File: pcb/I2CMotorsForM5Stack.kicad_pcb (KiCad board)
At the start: 2 copper layers, 60 x 50 mm, 26 parts, among them J1 free_holes, J3 Conn_01x06, J4 Conn_01x06, SW1 SW_DIP_x08, U1 TB6612FNG, U2 ATmega328PB-MU

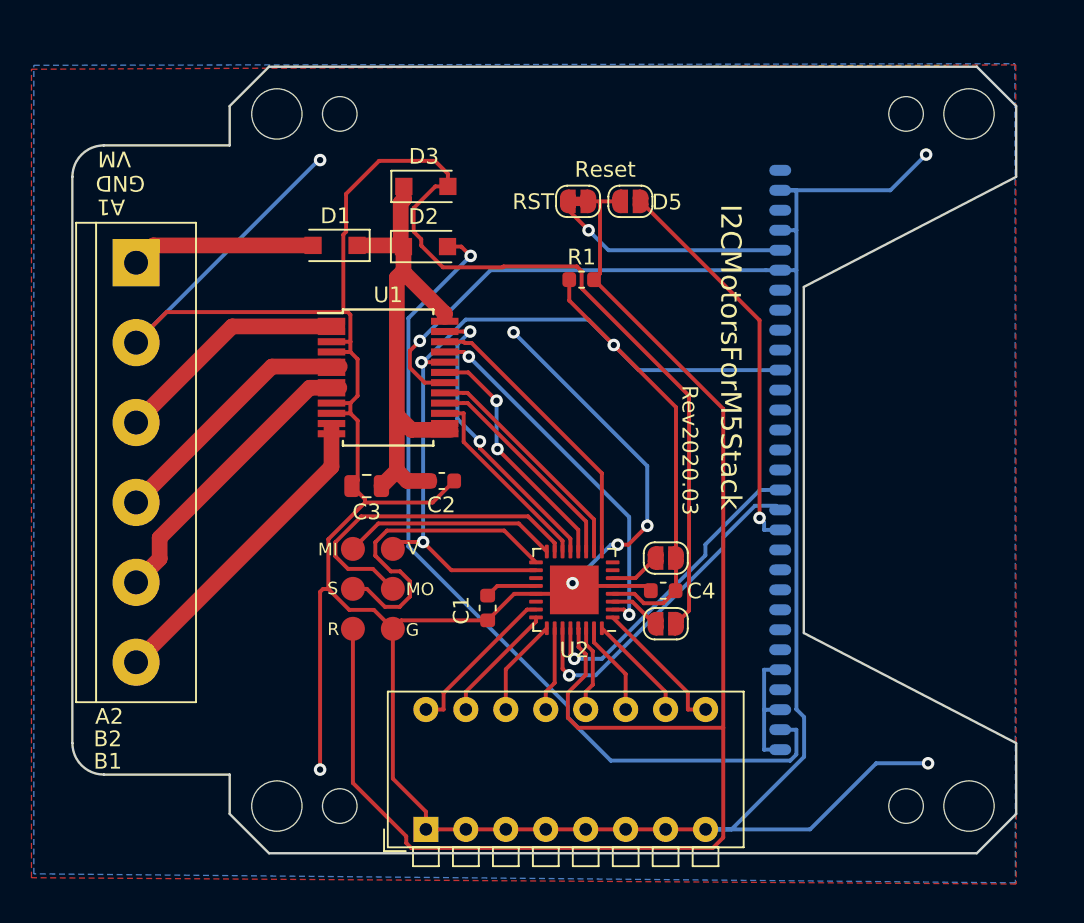
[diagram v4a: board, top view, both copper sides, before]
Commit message: Add connectors and address pads
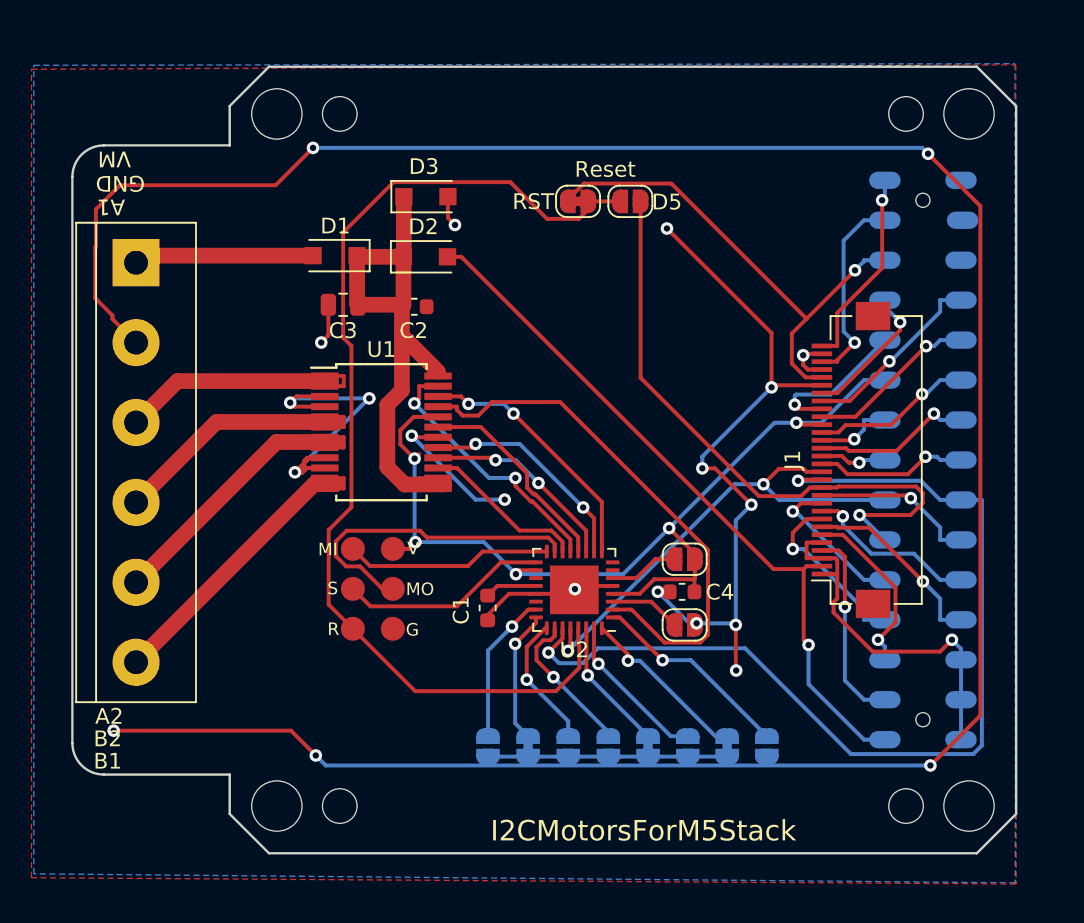
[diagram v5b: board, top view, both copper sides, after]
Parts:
- removed R1: 10k, Resistor_SMD:R_0603_1608Metric
- removed SW1: SW_DIP_x08, Button_Switch_THT:SW_DIP_SPSTx08_Piano_CTS_Series194-8MSTN_W7.62mm_P2.54mm
- added ADDR1: NO, Jumper:SolderJumper-2_P1.3mm_Open_RoundedPad1.0x1.5mm, B.Cu at (116.4, 93.2)
- added ADDR2: NC, Jumper:SolderJumper-2_P1.3mm_Bridged_RoundedPad1.0x1.5mm, B.Cu at (119.0, 93.2)
- added ADDR3: NO, Jumper:SolderJumper-2_P1.3mm_Open_RoundedPad1.0x1.5mm, B.Cu at (121.5, 93.2)
- added ADDR4: NO, Jumper:SolderJumper-2_P1.3mm_Open_RoundedPad1.0x1.5mm, B.Cu at (124.1, 93.2)
- added ADDR5: NC, Jumper:SolderJumper-2_P1.3mm_Bridged_RoundedPad1.0x1.5mm, B.Cu at (126.6, 93.2)
- added ADDR6: NO, Jumper:SolderJumper-2_P1.3mm_Open_RoundedPad1.0x1.5mm, B.Cu at (129.1, 93.2)
- added ADDR7: NC, Jumper:SolderJumper-2_P1.3mm_Bridged_RoundedPad1.0x1.5mm, B.Cu at (131.6, 93.2)
- added ADDR8: NO, Jumper:SolderJumper-2_P1.3mm_Open_RoundedPad1.0x1.5mm, B.Cu at (134.1, 93.2)
- added J2: 2x15socket, my-kicad-footprints:PinSocket_2x15_P2.54mm_Vertical_SMD_just_for_M5Stack_bottom, B.Cu at (144.1, 75.0)
- J1: value free_holes -> FFC_connector; footprint footprints:Pads_1x30_P1.27mm_Vertical -> Connector_FFC-FPC:Hirose_FH12-30S-0.5SH_1x30-1MP_P0.50mm_Horizontal; moved to F.Cu
- JP1: value Jumper_NC_Small -> NC
- JP2: value Jumper_NO_Small -> NO
- JP3, JP4: value NC -> NO
- moved J1 19.0 mm to (139.5, 75.0), turned to 90 degrees
- moved C3 11.6 mm to (107.2, 65.1)
- moved C2 11.2 mm to (111.7, 65.3)
- moved U1 3.50 mm to (109.6, 73.2)
- moved JP3 1.20 mm to (128.9, 85.5)
- moved JP4 1.20 mm to (128.9, 81.3)
- moved C4 1.20 mm to (128.8, 83.4)
- moved D3 0.65 mm to (112.5, 58.3)
- moved D1 0.65 mm to (106.7, 62.0)
- moved D2 0.65 mm to (112.4, 62.1)
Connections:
- J1 pad 1: /35 -> /HPWR
- J1 pad 10: /19 -> /13
- J1 pad 11: +3V3 -> /2
- J1 pad 12: /18 -> /5
- J1 pad 13: /1 -> /21
- J1 pad 14: /3 -> /22
- J1 pad 15: /17 -> /16
- J1 pad 16: /16 -> /17
- J1 pad 17: /22 -> /3
- J1 pad 18: /21 -> /1
- J1 pad 19: /5 -> /18
- J1 pad 2: GND -> +BATT
- J1 pad 20: /2 -> +3V3
- J1 pad 21: /13 -> /19
- J1 pad 22: /12 -> /26
- J1 pad 23: /0 -> /23
- J1 pad 24: /15 -> /25
- J1 pad 25: /34 -> GND
- J1 pad 26: /HPWR -> /RST
- J1 pad 27: +5V -> GND
- J1 pad 28: /HPWR -> /36
- J1 pad 29: +BATT -> GND
- J1 pad 3: /36 -> /HPWR
- J1 pad 30: /HPWR -> /35
- J1 pad 4: GND -> +5V
- J1 pad 5: /RST -> /HPWR
- J1 pad 6: GND -> /34
- J1 pad 7: /25 -> /15
- J1 pad 8: /23 -> /0
- J1 pad 9: /26 -> /12
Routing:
- net GND: track 311.0 -> 267.7 mm, vias 9 -> 22
- net /21: track 21.5 -> 62.5 mm, vias 1 -> 2
- net /SPI_RESET: track 98.1 -> 66.5 mm
- net /RST: track 15.1 -> 31.4 mm
- net /HPWR: track 8.16 -> 23.8 mm, vias 0 -> 1
- net /5: track 25.2 -> 39.9 mm
- net +3V3: track 75.4 -> 61.5 mm, vias 3 -> 5
- net /35: track 0.00 -> 12.8 mm, vias 0 -> 1
- net /36: track 0.00 -> 12.6 mm, vias 0 -> 1
- net +5V: track 0.00 -> 12.5 mm, vias 0 -> 1
- net /15: track 0.00 -> 12.1 mm, vias 0 -> 1
- net /23: track 0.00 -> 11.9 mm, vias 0 -> 1
- net /0: track 0.00 -> 11.4 mm, vias 0 -> 1
- net /34: track 0.00 -> 11.3 mm, vias 0 -> 1
- net /12: track 0.00 -> 11.0 mm, vias 0 -> 1
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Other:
- outline, holes or cut-outs redrawn
- board text added: "Rev2020.04"
- board text removed: "0/MK"
- board text removed: "1/T0"
- board text removed: "12/SK"
- board text removed: "13/WS"
- board text removed: "15/OUT"
- board text removed: "16/R2"
- board text removed: "17/T2"
- board text removed: "18/SCK"
- board text removed: "19/MI"
- board text removed: "2"
- board text removed: "21/SDA"
- board text removed: "22/SCL"
- board text removed: "23/MO"
- board text removed: "25/DA"
- board text removed: "26/DA"
- board text removed: "3/R0"
- board text removed: "34/IN"
- board text removed: "36/AD"
- board text removed: "3V3"
- board text removed: "5"
- board text removed: "5V"
- board text removed: "BAT"
- board text removed: "HPWR"
- board text removed: "Rev2020.03"

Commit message: Change start number for address pad
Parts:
- renumbered ADDR1 to ADDR0, ADDR2 to ADDR1, ADDR3 to ADDR2, ADDR4 to ADDR3, ADDR5 to ADDR4, ADDR6 to ADDR5, ADDR7 to ADDR6, ADDR8 to ADDR7
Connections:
- ADDR0 pad 2: /ADDR1 -> /ADDR0
- ADDR1 pad 2: /ADDR2 -> /ADDR1
- ADDR2 pad 2: /ADDR3 -> /ADDR2
- ADDR3 pad 2: /ADDR4 -> /ADDR3
- ADDR4 pad 2: /ADDR5 -> /ADDR4
- ADDR5 pad 2: /ADDR6 -> /ADDR5
- ADDR6 pad 2: /ADDR7 -> /ADDR6
- ADDR7 pad 2: /ADDR8 -> /ADDR7
- U2 pad 1: /ADDR8 -> /ADDR7
- U2 pad 23: /ADDR1 -> /ADDR0
- U2 pad 24: /ADDR2 -> /ADDR1
- U2 pad 25: /ADDR3 -> /ADDR2
- U2 pad 26: /ADDR4 -> /ADDR3
- U2 pad 30: /ADDR5 -> /ADDR4
- U2 pad 31: /ADDR6 -> /ADDR5
- U2 pad 32: /ADDR7 -> /ADDR6
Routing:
- net /ADDR8: track 12.9 -> 0.00 mm, vias 1 -> 0
- net /ADDR0: track 0.00 -> 10.0 mm, vias 0 -> 1
- net /ADDR7: track 11.0 -> 12.9 mm
- net /ADDR1: track 10.0 -> 8.44 mm
- net /ADDR5: track 8.49 -> 9.97 mm
- net /ADDR6: track 9.97 -> 11.0 mm
- net /ADDR4: track 9.50 -> 8.49 mm
- net /ADDR3: track 8.54 -> 9.50 mm

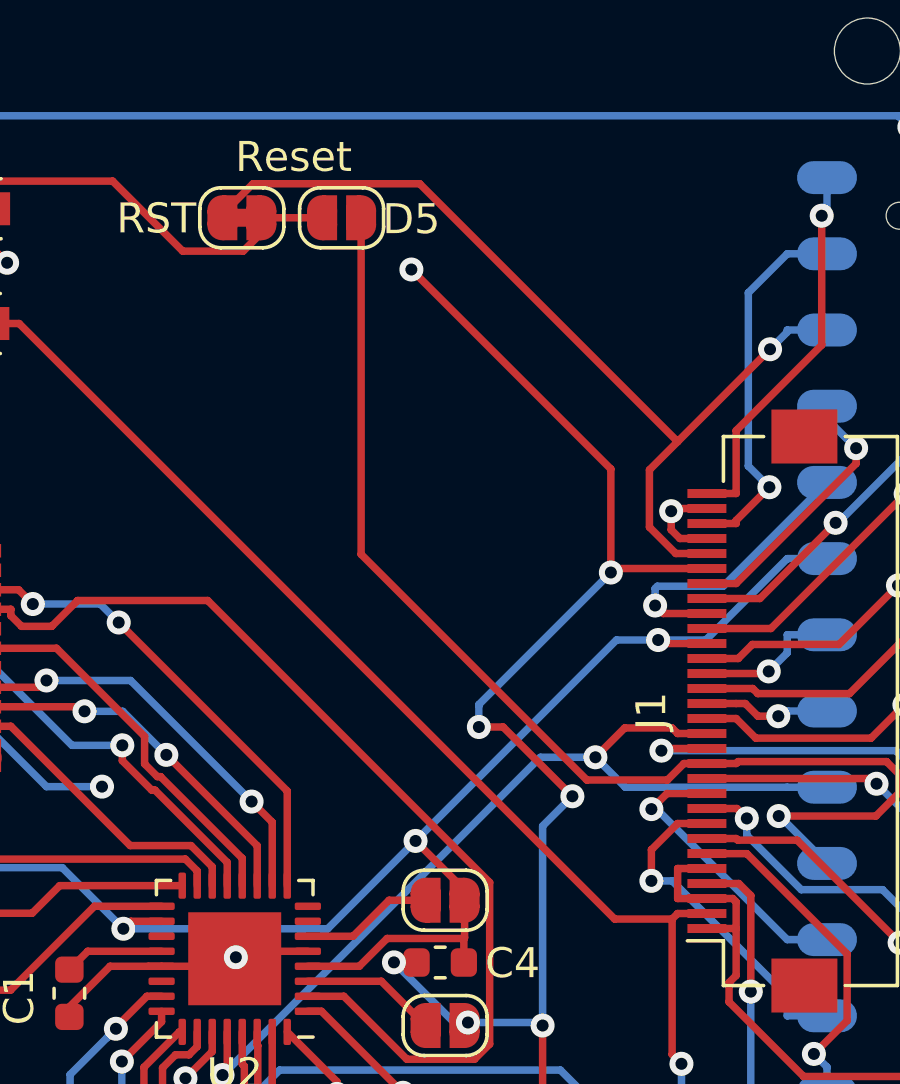
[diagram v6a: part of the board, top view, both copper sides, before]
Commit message: Correct accidentaly connected line
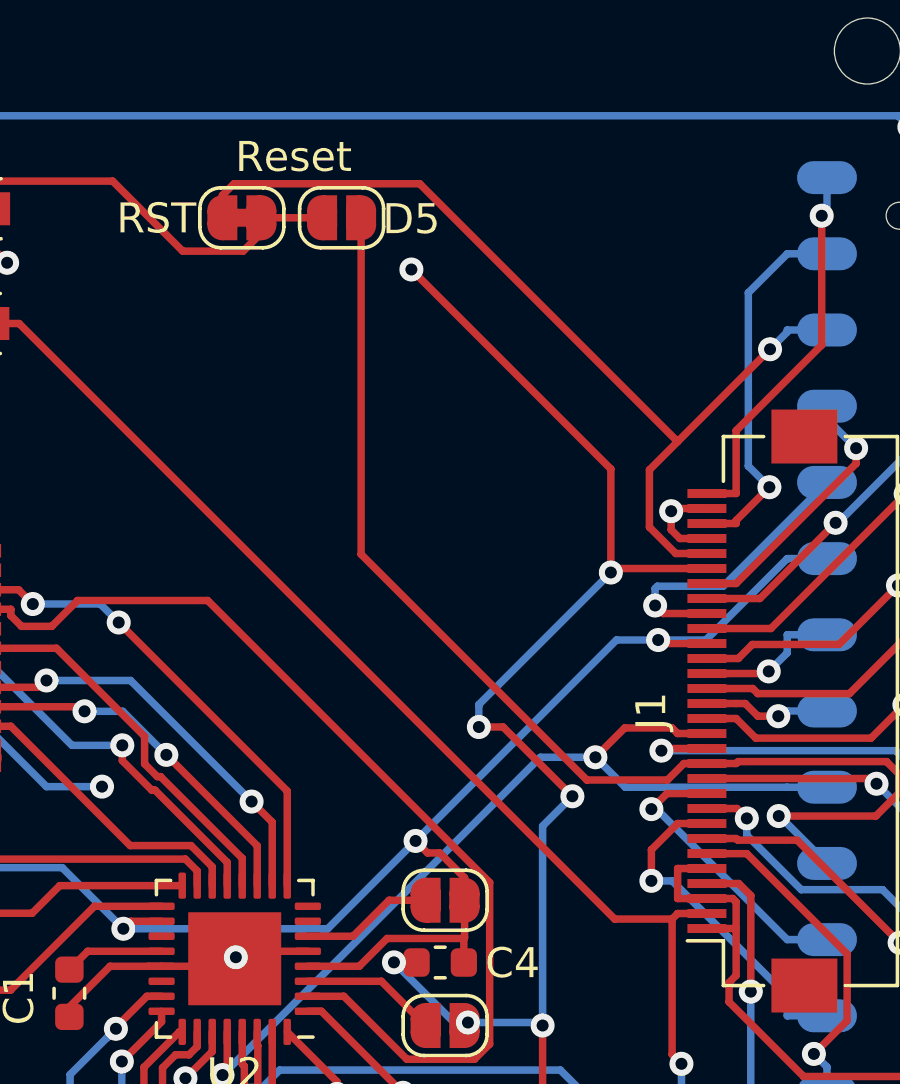
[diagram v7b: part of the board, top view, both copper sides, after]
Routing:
- net +3V3: track 61.5 -> 62.0 mm
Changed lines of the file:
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@@
     (thickness 1.6)
     (drawings 34)
-    (tracks 566)
+    (tracks 570)
     (zones 0)
     (modules 33)
@@
   (segment (start 118.1984 82.2582) (end 125.0109 82.2582) (width 0.25) (layer B.Cu) (net 4))
   (segment (start 125.0109 82.2582) (end 127.9388 79.3303) (width 0.25) (layer B.Cu) (net 4))
-  (segment (start 127.9388 79.3303) (end 129.574 80.9655) (width 0.25) (layer F.Cu) (net 4))
   (segment (start 129.574 80.9655) (end 129.574 81.3082) (width 0.25) (layer F.Cu) (net 4))
   (segment (start 129.5485 82.5814) (end 129.574 82.5559) (width 0.25) (layer F.Cu) (net 4))
@@
   (segment (start 110.848799 73.110199) (end 111.700798 72.2582) (width 0.25) (layer F.Cu) (net 4))
   (segment (start 110.848799 74.006299) (end 110.848799 73.110199) (width 0.25) (layer F.Cu) (net 4))
+  (segment (start 128.338799 79.730299) (end 127.9388 79.3303) (width 0.25) (layer F.Cu) (net 4))
+  (segment (start 128.743691 79.730299) (end 128.338799 79.730299) (width 0.25) (layer F.Cu) (net 4))
+  (segment (start 129.574 80.560608) (end 128.743691 79.730299) (width 0.25) (layer F.Cu) (net 4))
+  (segment (start 129.574 81.3082) (end 129.574 80.560608) (width 0.25) (layer F.Cu) (net 4))
   (segment (start 137.65 67.75) (end 138.6253 67.75) (width 0.25) (layer F.Cu) (net 5))
   (segment (start 141.4778 58.49) (end 141.654 58.3138) (width 0.25) (layer B.Cu) (net 5))
@@
   (via (at 139.7333 67.5391) (size 0.8) (layers F.Cu B.Cu) (net 6))
   (segment (start 139.7555 62.9409) (end 136.6747 66.0217) (width 0.25) (layer F.Cu) (net 7))
-  (segment (start 121.499 58.5582) (end 121.499 58.4443) (width 0.25) (layer F.Cu) (net 7))
-  (segment (start 121.499 58.4443) (end 122.519 57.4243) (width 0.25) (layer F.Cu) (net 7))
-  (segment (start 122.519 57.4243) (end 128.0773 57.4243) (width 0.25) (layer F.Cu) (net 7))
-  (segment (start 128.0773 57.4243) (end 136.6747 66.0217) (width 0.25) (layer F.Cu) (net 7))
   (segment (start 141.654 62.3) (end 140.3287 62.3) (width 0.25) (layer B.Cu) (net 7))
   (segment (start 139.7555 62.9409) (end 140.3287 62.3677) (width 0.25) (layer B.Cu) (net 7))
@@
   (segment (start 136.61359 69.75) (end 135.734599 68.871009) (width 0.25) (layer F.Cu) (net 7))
   (segment (start 137.65 69.75) (end 136.61359 69.75) (width 0.25) (layer F.Cu) (net 7))
+  (segment (start 121.499 58.5582) (end 121.499 58.4443) (width 0.25) (layer F.Cu) (net 7))
+  (segment (start 121.499 57.810608) (end 121.499 58.5582) (width 0.25) (layer F.Cu) (net 7))
+  (segment (start 121.885308 57.4243) (end 121.499 57.810608) (width 0.25) (layer F.Cu) (net 7))
+  (segment (start 128.0773 57.4243) (end 121.885308 57.4243) (width 0.25) (layer F.Cu) (net 7))
+  (segment (start 136.6747 66.0217) (end 128.0773 57.4243) (width 0.25) (layer F.Cu) (net 7))
   (segment (start 142.6244 66.239) (end 142.6244 66.7509) (width 0.25) (layer F.Cu) (net 8))
   (segment (start 142.6244 66.7509) (end 138.6253 70.75) (width 0.25) (layer F.Cu) (net 8))
@@
     (connect_pads (clearance 0.508))
     (min_thickness 0.254)
-    (fill (arc_segments 32) (thermal_gap 0.508) (thermal_bridge_width 0.508))
+    (fill yes (arc_segments 32) (thermal_gap 0.508) (thermal_bridge_width 0.508))
     (polygon
       (pts
@@
     (connect_pads (clearance 0.508))
     (min_thickness 0.254)
-    (fill (arc_segments 32) (thermal_gap 0.508) (thermal_bridge_width 0.508))
+    (fill yes (arc_segments 32) (thermal_gap 0.508) (thermal_bridge_width 0.508))
     (polygon
       (pts
